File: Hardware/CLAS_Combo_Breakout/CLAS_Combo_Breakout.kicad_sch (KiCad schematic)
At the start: 86 parts, among them J1 USB_C_Receptacle_USB2.0, J2 ZED, J3 NEO, J4 USB_C_Receptacle_USB2.0, J5 Conn_SMA, U1 USBLC6-2P6, U10 NT1191GEAE3S, U2 ZED-F9P, U3 NEO-D9C-00B, U4 USBLC6-2P6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

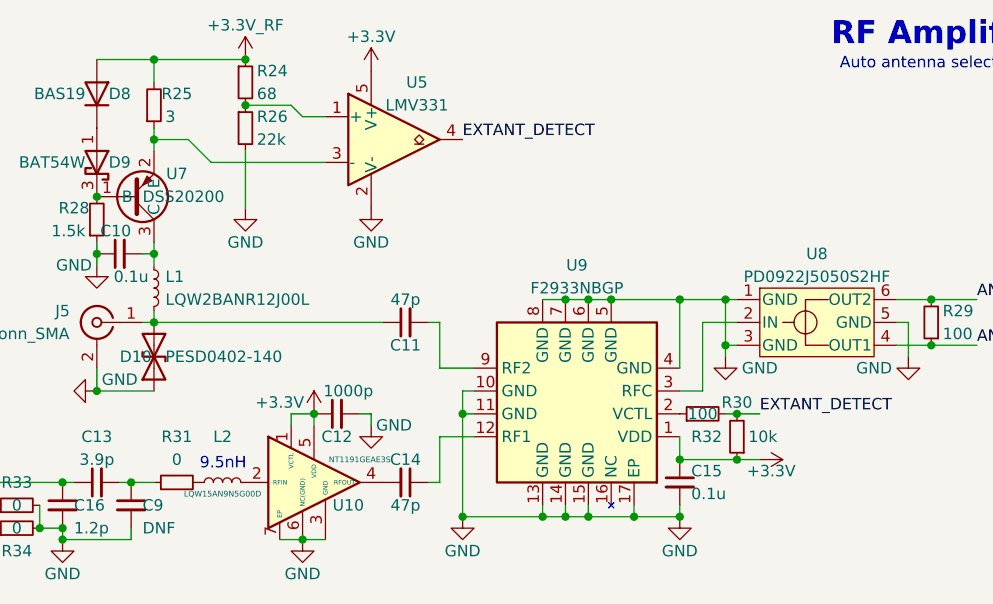
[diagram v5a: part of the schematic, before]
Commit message: トランジスタの記号をQに変更、REFを整理
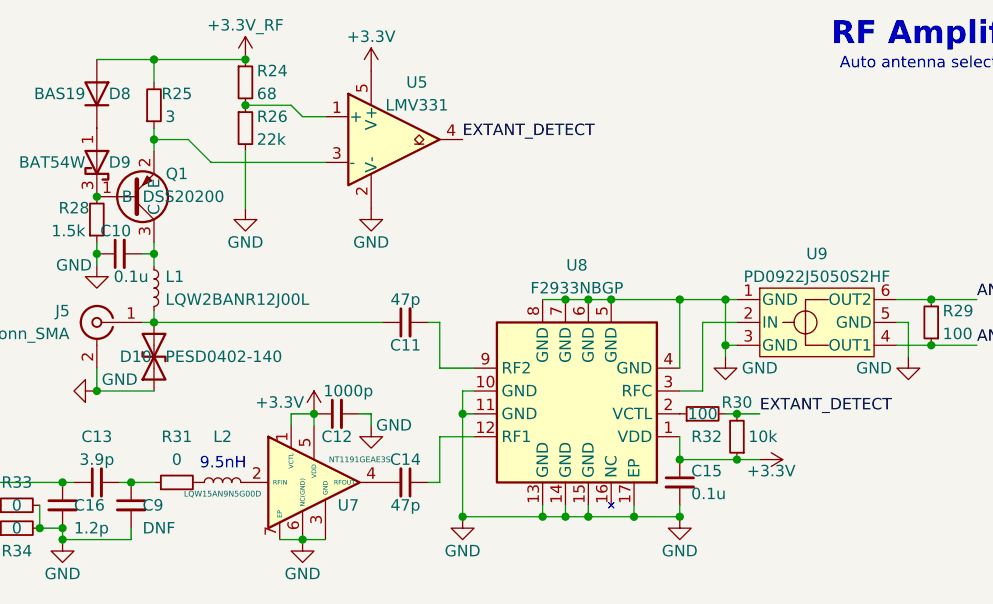
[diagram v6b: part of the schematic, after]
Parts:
- renumbered U7 to Q1, U10 to U7, U9 to U8, U8 to U9
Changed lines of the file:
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@@
   (symbol (lib_id "PD0922J5050S2HF:PD0922J5050S2HF") (at 123.19 167.64 0) (unit 1)
     (in_bom yes) (on_board yes)
-    (property "Reference" "U8" (id 0) (at 123.19 160.02 0))
+    (property "Reference" "U9" (id 0) (at 123.19 160.02 0))
     (property "Value" "PD0922J5050S2HF" (id 1) (at 123.19 162.56 0))
     (property "Footprint" "PD0922J5050S2HF:PD0922J5050S2HF_ANA" (id 2) (at 123.19 175.26 0)
@@
   (symbol (lib_id "NT1191GEAE3S:NT1191GEAE3S") (at 66.04 185.42 0) (unit 1)
     (in_bom yes) (on_board yes)
-    (property "Reference" "U10" (id 0) (at 71.12 187.96 0))
+    (property "Reference" "U7" (id 0) (at 71.12 187.96 0))
     (property "Value" "NT1191GEAE3S" (id 1) (at 72.39 182.88 0)
       (effects (font (size 0.635 0.635)))
@@
   (symbol (lib_id "DSS20200L-7:DSS20200L-7") (at 48.26 153.67 0) (mirror x) (unit 1)
     (in_bom yes) (on_board yes)
-    (property "Reference" "U7" (id 0) (at 52.07 151.13 0))
+    (property "Reference" "Q1" (id 0) (at 52.07 151.13 0))
     (property "Value" "DSS20200" (id 1) (at 48.26 153.67 0)
       (effects (font (size 1.27 1.27)) (justify left))
@@
   (symbol (lib_id "F2933NBGP:F2933NBGP") (at 96.52 176.53 180) (unit 1)
     (in_bom yes) (on_board yes)
-    (property "Reference" "U9" (id 0) (at 96.52 161.29 0))
+    (property "Reference" "U8" (id 0) (at 96.52 161.29 0))
     (property "Value" "F2933NBGP" (id 1) (at 96.52 163.83 0))
     (property "Footprint" "F2933NBGP:F2933NBGP" (id 2) (at 107.95 180.34 0)
@@
       (reference "L2") (unit 1) (value "LQW15AN9N5G00D") (footprint "LQW15AN9N5G00D:LQW15AN9N5G00D")
     )
+    (path "/d4e2c2b1-f9fd-4713-9fee-187d649c8dce"
+      (reference "Q1") (unit 1) (value "DSS20200") (footprint "DSS20200L-7:DSS20200L-7")
+    )
     (path "/9e101cf8-88ad-4ea8-978c-246e3974522f"
       (reference "R1") (unit 1) (value "33") (footprint "Resistor_SMD:R_0603_1608Metric")
@@
       (reference "U6") (unit 1) (value "AP2112K-3.3") (footprint "Package_TO_SOT_SMD:SOT-23-5")
     )
-    (path "/d4e2c2b1-f9fd-4713-9fee-187d649c8dce"
-      (reference "U7") (unit 1) (value "DSS20200") (footprint "DSS20200L-7:DSS20200L-7")
+    (path "/227e032c-a965-4181-9cad-30c22164f63e"
+      (reference "U7") (unit 1) (value "NT1191GEAE3S") (footprint "NT1191GEAE3S:NT1191GEAE3S")
+    )
+    (path "/e370f382-0910-4fb6-8285-1d9371eb5cba"
+      (reference "U8") (unit 1) (value "F2933NBGP") (footprint "F2933NBGP:F2933NBGP")
     )
     (path "/18c0aa5d-674b-40ff-9786-65c2af4b8f3a"
-      (reference "U8") (unit 1) (value "PD0922J5050S2HF") (footprint "PD0922J5050S2HF:PD0922J5050S2HF_ANA")
-    )
-    (path "/e370f382-0910-4fb6-8285-1d9371eb5cba"
-      (reference "U9") (unit 1) (value "F2933NBGP") (footprint "F2933NBGP:F2933NBGP")
-    )
-    (path "/227e032c-a965-4181-9cad-30c22164f63e"
-      (reference "U10") (unit 1) (value "NT1191GEAE3S") (footprint "NT1191GEAE3S:NT1191GEAE3S")
-    )
-  )
+      (reference "U9") (unit 1) (value "PD0922J5050S2HF") (footprint "PD0922J5050S2HF:PD0922J5050S2HF_ANA")
+    )
+  )

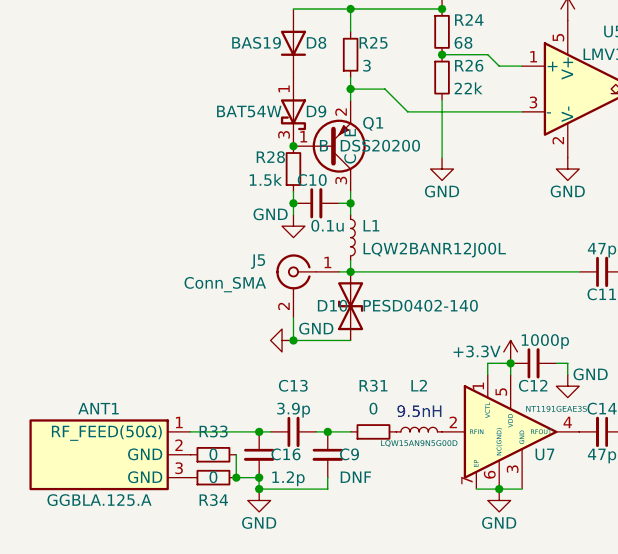
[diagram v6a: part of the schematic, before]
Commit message: MMCXのフットプリントを作成　ピン表示のシルクの位置調整
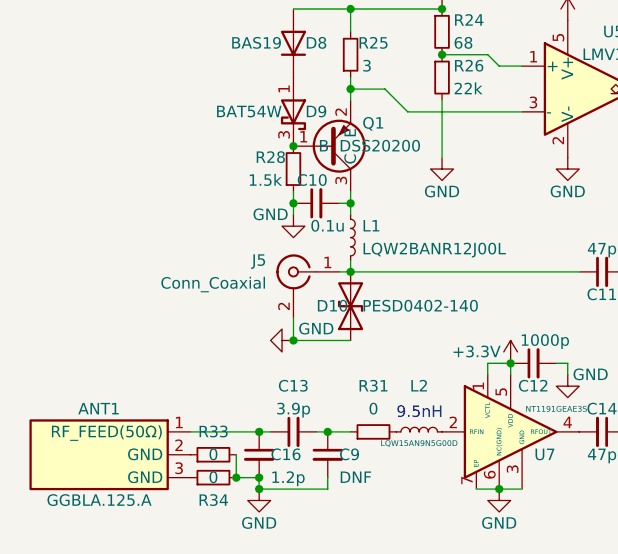
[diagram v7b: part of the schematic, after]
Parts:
- J5: value Conn_SMA -> Conn_Coaxial; footprint Connector_Coaxial:U.FL_Hirose_U.FL-R-SMT-1_Vertical -> Connector_Coaxial_extlib:0734152063
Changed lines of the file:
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@@
     (in_bom yes) (on_board yes)
     (property "Reference" "J5" (id 0) (at 39.37 166.37 0))
-    (property "Value" "Conn_SMA" (id 1) (at 35.56 168.91 0))
-    (property "Footprint" "Connector_Coaxial:U.FL_Hirose_U.FL-R-SMT-1_Vertical" (id 2) (at 43.18 167.64 0)
+    (property "Value" "Conn_Coaxial" (id 1) (at 34.29 168.91 0))
+    (property "Footprint" "Connector_Coaxial_extlib:0734152063" (id 2) (at 43.18 167.64 0)
       (effects (font (size 1.27 1.27)) hide)
     )
@@
     )
     (path "/c1f8d42f-0e23-4789-b87b-a02b45b47937"
-      (reference "J5") (unit 1) (value "Conn_SMA") (footprint "Connector_Coaxial:U.FL_Hirose_U.FL-R-SMT-1_Vertical")
+      (reference "J5") (unit 1) (value "Conn_Coaxial") (footprint "Connector_Coaxial_extlib:0734152063")
     )
     (path "/b54126b3-7985-4549-85a9-fc253ef56032"

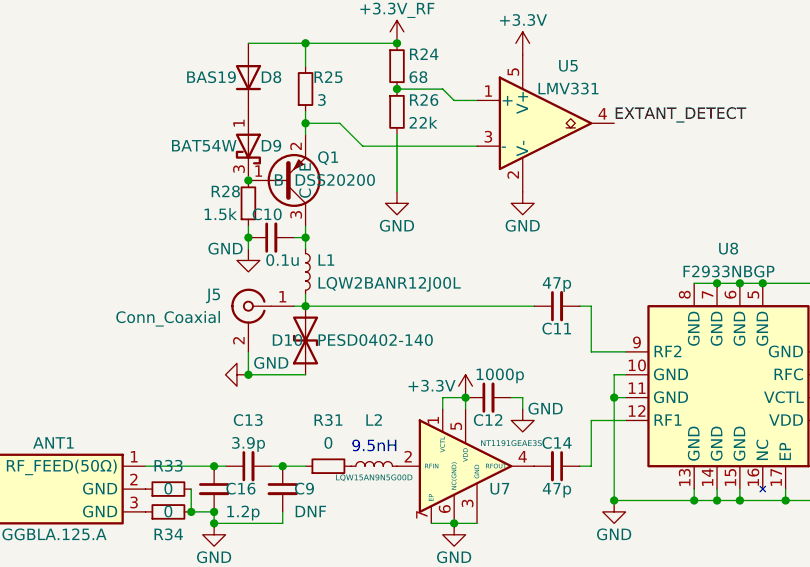
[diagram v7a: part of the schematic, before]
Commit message: インダクタを変更　フットプリントを追加
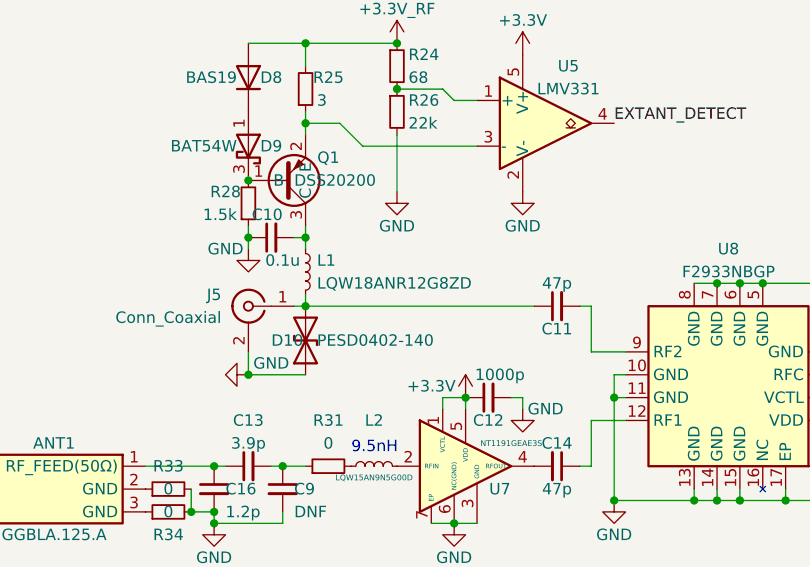
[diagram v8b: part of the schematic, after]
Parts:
- L1: value LQW2BANR12J00L -> LQW18ANR12G8ZD; footprint LQW2BANR12J00L:LQW2BANR12J00L -> LQW18ANR12G8ZD:LQW18ANR12G8ZD
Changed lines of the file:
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@@
       (effects (font (size 1.27 1.27)) (justify left))
     )
-    (property "Value" "LQW2BANR12J00L" (id 1) (at 50.8 165.0999 0)
-      (effects (font (size 1.27 1.27)) (justify left))
-    )
-    (property "Footprint" "LQW2BANR12J00L:LQW2BANR12J00L" (id 2) (at 49.53 163.83 0)
+    (property "Value" "LQW18ANR12G8ZD" (id 1) (at 50.8 165.0999 0)
+      (effects (font (size 1.27 1.27)) (justify left))
+    )
+    (property "Footprint" "LQW18ANR12G8ZD:LQW18ANR12G8ZD" (id 2) (at 49.53 163.83 0)
       (effects (font (size 1.27 1.27)) hide)
     )
@@
     )
     (path "/be16f664-0619-4856-937a-e239b591adad"
-      (reference "L1") (unit 1) (value "LQW2BANR12J00L") (footprint "LQW2BANR12J00L:LQW2BANR12J00L")
+      (reference "L1") (unit 1) (value "LQW18ANR12G8ZD") (footprint "LQW18ANR12G8ZD:LQW18ANR12G8ZD")
     )
     (path "/cb151227-edd6-414d-a78a-15ea2070f06b"
